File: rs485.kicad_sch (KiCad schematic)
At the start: 1 part

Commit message: add
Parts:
- added J1: Conn_01x04_Pin, symbol Connector:Conn_01x04_Pin
- added J2: Conn_01x04_Socket, symbol Connector:Conn_01x04_Socket
- added U2: SN74CB3Q3384APW, Package_SO:TSSOP-24_4.4x7.8mm_P0.65mm, symbol 74xx:SN74CB3Q3384APW
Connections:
- net at U1.1 (R): now also U1.4 (D), U2.3 (1A1)
- net at U1.2 (RE~): now also U1.3 (DE), U2.4 (1A2)
- net GND: now reaches U1.5 (GND)
- net GND: now also J1.4 (Pin_4), U2.12 (GND)
- net at U1.6 (B): now also J1.2 (Pin_2)
- net at U1.7 (A): now also J1.1 (Pin_1)
- net +5V: now reaches U1.8 (VCC)
- net +5V: now also J1.3 (Pin_3), U2.24 (VCC)
- new net: J2.3 (Pin_3), U2.1 (~{1OE})
- new net: J2.4 (Pin_4), U2.13 (~{2OE})
- new net: J2.1 (Pin_1), U2.2 (1B1)
- new net: J2.2 (Pin_2), U2.5 (1B2)

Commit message: sch of.
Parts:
- removed J2: Conn_01x04_Socket, symbol Connector:Conn_01x04_Socket
- added J2: Conn_01x04_Pin, symbol Connector:Conn_01x04_Pin
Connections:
- net GND: now also J2.1 (Pin_1); no longer J1.4 (Pin_4)
- net at U2.1 (~{1OE}): now also J1.3 (Pin_3)
- net at U2.13 (~{2OE}): now also J1.4 (Pin_4)
- net at U2.2 (1B1): now also J1.1 (Pin_1)
- net at U1.1 (R), U1.4 (D): now also U2.4 (1A2); no longer U2.3 (1A1)
- net at U1.2 (RE~), U1.3 (DE): now also U2.3 (1A1); no longer U2.4 (1A2)
- net at U2.5 (1B2): now also J1.2 (Pin_2)
- net at U1.6 (B): now also J2.3 (Pin_3); no longer J1.2 (Pin_2)
- net at U1.7 (A): now also J2.4 (Pin_4); no longer J1.1 (Pin_1)
- net +5V renamed VCC
- net VCC: now also J2.2 (Pin_2); no longer J1.3 (Pin_3)

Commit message: sch ok.
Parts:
- removed J1, J2: Conn_01x04_Pin, symbol Connector:Conn_01x04_Pin
- added J1, J3: Conn_01x12_Pin, symbol Connector:Conn_01x12_Pin
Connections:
- net GND: now also J1.9 (Pin_9)
- net VCC: now also J1.10 (Pin_10)
- net at U1.6 (B): now also J1.11 (Pin_11)
- net at U1.7 (A): now also J1.12 (Pin_12)
- net at U2.2 (1B1): now also J3.1 (Pin_1)
- net at U2.5 (1B2): now also J3.2 (Pin_2)
- net at U2.1 (~{1OE}): now also J3.11 (Pin_11)
- net at U2.13 (~{2OE}): now also J3.12 (Pin_12)
- net at U2.10 (1B5): now also J1.6 (Pin_6)
- net at U2.11 (1A5): now also J3.5 (Pin_5)
- net at U2.14 (2A1): now also J3.6 (Pin_6)
- net at U2.15 (2B1): now also J1.5 (Pin_5)
- net at U2.16 (2B2): now also J1.4 (Pin_4)
- net at U2.17 (2A2): now also J3.7 (Pin_7)
- net at U2.18 (2A3): now also J3.8 (Pin_8)
- net at U2.19 (2B3): now also J1.3 (Pin_3)
- net at U2.20 (2B4): now also J1.2 (Pin_2)
- net at U2.21 (2A4): now also J3.9 (Pin_9)
- net at U2.22 (2A5): now also J3.10 (Pin_10)
- net at U2.23 (2B5): now also J1.1 (Pin_1)
- net at U2.6 (1B3): now also J1.8 (Pin_8)
- net at U2.7 (1A3): now also J3.3 (Pin_3)
- net at U2.8 (1A4): now also J3.4 (Pin_4)
- net at U2.9 (1B4): now also J1.7 (Pin_7)

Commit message: up/.
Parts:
- U1: footprint (none) -> SOIC127P600X175-8N:SOIC127P600X175-8N
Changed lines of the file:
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@@
       (effects (font (size 1.27 1.27)))
     )
-    (property "Footprint" "" (at 114.3 54.61 0)
+    (property "Footprint" "SOIC127P600X175-8N:SOIC127P600X175-8N" (at 114.3 54.61 0)
       (effects (font (size 1.27 1.27)) hide)
     )

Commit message: add pcb file.
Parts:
- J1, J3: footprint (none) -> Connector_PinHeader_2.54mm:PinHeader_1x12_P2.54mm_Vertical
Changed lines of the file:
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@@
       (effects (font (size 1.27 1.27)))
     )
-    (property "Footprint" "" (at 41.91 96.52 0)
+    (property "Footprint" "Connector_PinHeader_2.54mm:PinHeader_1x12_P2.54mm_Vertical" (at 41.91 96.52 0)
       (effects (font (size 1.27 1.27)) hide)
     )
@@
       (effects (font (size 1.27 1.27)) (justify right))
     )
-    (property "Footprint" "" (at 204.47 74.93 0)
+    (property "Footprint" "Connector_PinHeader_2.54mm:PinHeader_1x12_P2.54mm_Vertical" (at 204.47 74.93 0)
       (effects (font (size 1.27 1.27)) hide)
     )

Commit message: pcb
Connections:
- net VCC: now also J1.12 (Pin_12); no longer J1.10 (Pin_10)
- net at U1.6 (B): now also J1.10 (Pin_10); no longer J1.11 (Pin_11)
- net at U1.7 (A): now also J1.11 (Pin_11); no longer J1.12 (Pin_12)
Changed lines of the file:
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@@
     (stroke (width 0) (type default))
   )
-  (wire (pts (xy 154.94 57.15) (xy 173.99 57.15))
+  (wire (pts (xy 154.94 57.15) (xy 179.07 57.15))
     (stroke (width 0) (type default))
   )
@@
     (stroke (width 0) (type default))
   )
+  (wire (pts (xy 175.26 59.69) (xy 175.26 62.23))
+    (stroke (width 0) (type default))
+  )
   (wire (pts (xy 128.27 102.87) (xy 176.53 102.87))
     (stroke (width 0) (type default))
@@
     (stroke (width 0) (type default))
   )
+  (wire (pts (xy 165.1 64.77) (xy 165.1 62.23))
+    (stroke (width 0) (type default))
+  )
   (wire (pts (xy 93.98 85.09) (xy 93.98 87.63))
     (stroke (width 0) (type default))
@@
     (stroke (width 0) (type default))
   )
+  (wire (pts (xy 123.19 59.69) (xy 175.26 59.69))
+    (stroke (width 0) (type default))
+  )
+  (wire (pts (xy 175.26 62.23) (xy 199.39 62.23))
+    (stroke (width 0) (type default))
+  )
   (wire (pts (xy 90.17 104.14) (xy 90.17 102.87))
     (stroke (width 0) (type default))
   )
-  (wire (pts (xy 123.19 62.23) (xy 199.39 62.23))
-    (stroke (width 0) (type default))
-  )
   (wire (pts (xy 46.99 109.22) (xy 88.9 109.22))
     (stroke (width 0) (type default))
@@
     (stroke (width 0) (type default))
   )
-  (wire (pts (xy 173.99 64.77) (xy 199.39 64.77))
-    (stroke (width 0) (type default))
-  )
   (wire (pts (xy 142.24 127) (xy 142.24 138.43))
     (stroke (width 0) (type default))
@@
     (stroke (width 0) (type default))
   )
+  (wire (pts (xy 179.07 59.69) (xy 179.07 57.15))
+    (stroke (width 0) (type default))
+  )
   (wire (pts (xy 180.34 105.41) (xy 180.34 87.63))
     (stroke (width 0) (type default))
@@
     (stroke (width 0) (type default))
   )
-  (wire (pts (xy 173.99 57.15) (xy 173.99 64.77))
-    (stroke (width 0) (type default))
-  )
   (wire (pts (xy 167.64 95.25) (xy 167.64 77.47))
     (stroke (width 0) (type default))
@@
     (stroke (width 0) (type default))
   )
+  (wire (pts (xy 199.39 64.77) (xy 165.1 64.77))
+    (stroke (width 0) (type default))
+  )
   (wire (pts (xy 105.41 59.69) (xy 100.33 59.69))
     (stroke (width 0) (type default))
@@
     (stroke (width 0) (type default))
   )
+  (wire (pts (xy 199.39 59.69) (xy 179.07 59.69))
+    (stroke (width 0) (type default))
+  )
   (wire (pts (xy 162.56 72.39) (xy 199.39 72.39))
     (stroke (width 0) (type default))
@@
     (stroke (width 0) (type default))
   )
-  (wire (pts (xy 123.19 59.69) (xy 199.39 59.69))
-    (stroke (width 0) (type default))
-  )
   (wire (pts (xy 80.01 90.17) (xy 80.01 93.98))
     (stroke (width 0) (type default))
@@
     (stroke (width 0) (type default))
   )
+  (wire (pts (xy 165.1 62.23) (xy 123.19 62.23))
+    (stroke (width 0) (type default))
+  )

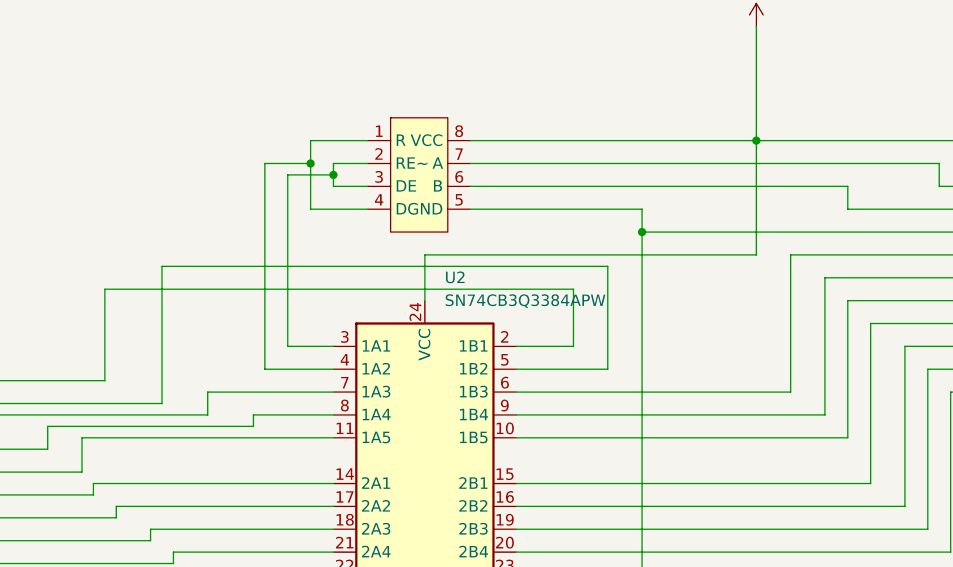
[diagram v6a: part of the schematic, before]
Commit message: 之前的没问题，现在重新设计，重新制作一个，加电源稳压的电容。
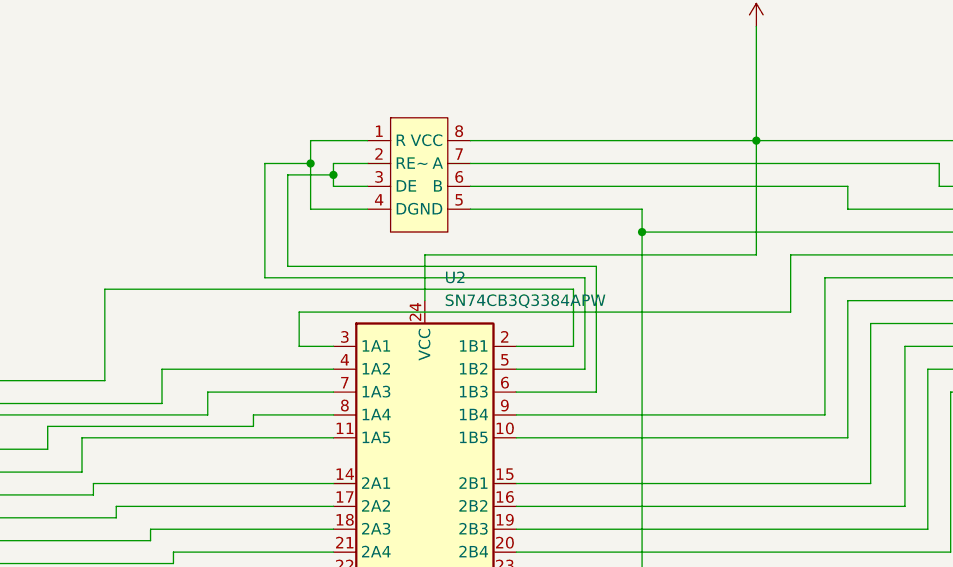
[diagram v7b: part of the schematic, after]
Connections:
- net at U1.1 (R), U1.4 (D): now also U2.5 (1B2); no longer U2.4 (1A2)
- net at U1.2 (RE~), U1.3 (DE): now also U2.6 (1B3); no longer U2.3 (1A1)
- net at J3.2 (Pin_2): now also U2.4 (1A2); no longer U2.5 (1B2)
- net at J1.8 (Pin_8): now also U2.3 (1A1); no longer U2.6 (1B3)
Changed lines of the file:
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@@
   (junction (at 107.95 60.96) (diameter 0) (color 0 0 0 0)
   )
+  (junction (at 142.24 127) (diameter 0) (color 0 0 0 0)
+  )
   (junction (at 105.41 59.69) (diameter 0) (color 0 0 0 0)
   )
-  (junction (at 142.24 127) (diameter 0) (color 0 0 0 0)
-  )
   (junction (at 142.24 67.31) (diameter 0) (color 0 0 0 0)
   )
-  (wire (pts (xy 138.43 71.12) (xy 88.9 71.12))
-    (stroke (width 0) (type default))
-  )
   (wire (pts (xy 69.85 88.9) (xy 46.99 88.9))
     (stroke (width 0) (type default))
@@
     (stroke (width 0) (type default))
   )
+  (wire (pts (xy 158.75 76.2) (xy 104.14 76.2))
+    (stroke (width 0) (type default))
+  )
   (wire (pts (xy 142.24 64.77) (xy 142.24 67.31))
     (stroke (width 0) (type default))
@@
     (stroke (width 0) (type default))
   )
-  (wire (pts (xy 107.95 80.01) (xy 102.87 80.01))
-    (stroke (width 0) (type default))
-  )
   (wire (pts (xy 107.95 95.25) (xy 81.28 95.25))
     (stroke (width 0) (type default))
@@
     (stroke (width 0) (type default))
   )
+  (wire (pts (xy 102.87 60.96) (xy 102.87 71.12))
+    (stroke (width 0) (type default))
+  )
   (wire (pts (xy 105.41 57.15) (xy 105.41 59.69))
     (stroke (width 0) (type default))
@@
     (stroke (width 0) (type default))
   )
-  (wire (pts (xy 88.9 71.12) (xy 88.9 86.36))
+  (wire (pts (xy 134.62 73.66) (xy 82.55 73.66))
+    (stroke (width 0) (type default))
+  )
+  (wire (pts (xy 107.95 97.79) (xy 83.82 97.79))
+    (stroke (width 0) (type default))
+  )
+  (wire (pts (xy 162.56 87.63) (xy 162.56 72.39))
+    (stroke (width 0) (type default))
+  )
+  (wire (pts (xy 105.41 64.77) (xy 111.76 64.77))
+    (stroke (width 0) (type default))
+  )
+  (wire (pts (xy 137.16 71.12) (xy 137.16 85.09))
+    (stroke (width 0) (type default))
+  )
+  (wire (pts (xy 173.99 100.33) (xy 173.99 82.55))
+    (stroke (width 0) (type default))
+  )
+  (wire (pts (xy 107.95 90.17) (xy 80.01 90.17))
     (stroke (width 0) (type default))
   )
@@
     (stroke (width 0) (type default))
   )
-  (wire (pts (xy 134.62 73.66) (xy 82.55 73.66))
-    (stroke (width 0) (type default))
-  )
-  (wire (pts (xy 107.95 97.79) (xy 83.82 97.79))
-    (stroke (width 0) (type default))
-  )
-  (wire (pts (xy 162.56 87.63) (xy 162.56 72.39))
-    (stroke (width 0) (type default))
-  )
-  (wire (pts (xy 105.41 64.77) (xy 111.76 64.77))
-    (stroke (width 0) (type default))
-  )
-  (wire (pts (xy 173.99 100.33) (xy 173.99 82.55))
-    (stroke (width 0) (type default))
-  )
-  (wire (pts (xy 107.95 90.17) (xy 80.01 90.17))
-    (stroke (width 0) (type default))
-  )
   (wire (pts (xy 134.62 80.01) (xy 134.62 73.66))
     (stroke (width 0) (type default))
@@
     (stroke (width 0) (type default))
   )
-  (wire (pts (xy 128.27 82.55) (xy 138.43 82.55))
-    (stroke (width 0) (type default))
-  )
   (wire (pts (xy 80.01 93.98) (xy 46.99 93.98))
     (stroke (width 0) (type default))
   )
+  (wire (pts (xy 102.87 71.12) (xy 137.16 71.12))
+    (stroke (width 0) (type default))
+  )
   (wire (pts (xy 107.95 110.49) (xy 88.9 110.49))
     (stroke (width 0) (type default))
   )
-  (wire (pts (xy 138.43 71.12) (xy 138.43 82.55))
-    (stroke (width 0) (type default))
-  )
   (wire (pts (xy 176.53 102.87) (xy 176.53 85.09))
     (stroke (width 0) (type default))
@@
     (stroke (width 0) (type default))
   )
-  (wire (pts (xy 158.75 85.09) (xy 158.75 69.85))
+  (wire (pts (xy 88.9 82.55) (xy 88.9 86.36))
     (stroke (width 0) (type default))
   )
@@
     (stroke (width 0) (type default))
   )
-  (wire (pts (xy 102.87 80.01) (xy 102.87 60.96))
+  (wire (pts (xy 100.33 59.69) (xy 105.41 59.69))
     (stroke (width 0) (type default))
   )
@@
     (stroke (width 0) (type default))
   )
+  (wire (pts (xy 100.33 72.39) (xy 100.33 59.69))
+    (stroke (width 0) (type default))
+  )
   (wire (pts (xy 165.1 90.17) (xy 165.1 74.93))
     (stroke (width 0) (type default))
@@
     (stroke (width 0) (type default))
   )
+  (wire (pts (xy 104.14 76.2) (xy 104.14 80.01))
+    (stroke (width 0) (type default))
+  )
+  (wire (pts (xy 128.27 82.55) (xy 135.89 82.55))
+    (stroke (width 0) (type default))
+  )
   (wire (pts (xy 128.27 80.01) (xy 134.62 80.01))
     (stroke (width 0) (type default))
@@
     (stroke (width 0) (type default))
   )
+  (wire (pts (xy 104.14 80.01) (xy 107.95 80.01))
+    (stroke (width 0) (type default))
+  )
   (wire (pts (xy 99.06 88.9) (xy 76.2 88.9))
     (stroke (width 0) (type default))
   )
+  (wire (pts (xy 137.16 85.09) (xy 128.27 85.09))
+    (stroke (width 0) (type default))
+  )
   (wire (pts (xy 93.98 87.63) (xy 69.85 87.63))
     (stroke (width 0) (type default))
@@
     (stroke (width 0) (type default))
   )
+  (wire (pts (xy 88.9 82.55) (xy 107.95 82.55))
+    (stroke (width 0) (type default))
+  )
   (wire (pts (xy 154.94 57.15) (xy 123.19 57.15))
     (stroke (width 0) (type default))
   )
-  (wire (pts (xy 100.33 82.55) (xy 107.95 82.55))
-    (stroke (width 0) (type default))
-  )
   (wire (pts (xy 88.9 109.22) (xy 88.9 110.49))
     (stroke (width 0) (type default))
   )
+  (wire (pts (xy 158.75 69.85) (xy 158.75 76.2))
+    (stroke (width 0) (type default))
+  )
   (wire (pts (xy 167.64 95.25) (xy 167.64 77.47))
     (stroke (width 0) (type default))
   )
-  (wire (pts (xy 100.33 59.69) (xy 100.33 82.55))
-    (stroke (width 0) (type default))
-  )
-  (wire (pts (xy 128.27 85.09) (xy 158.75 85.09))
+  (wire (pts (xy 135.89 72.39) (xy 100.33 72.39))
     (stroke (width 0) (type default))
   )
@@
     (stroke (width 0) (type default))
   )
-  (wire (pts (xy 105.41 59.69) (xy 100.33 59.69))
-    (stroke (width 0) (type default))
-  )
   (wire (pts (xy 92.71 105.41) (xy 92.71 106.68))
     (stroke (width 0) (type default))
@@
     (stroke (width 0) (type default))
   )
+  (wire (pts (xy 135.89 82.55) (xy 135.89 72.39))
+    (stroke (width 0) (type default))
+  )

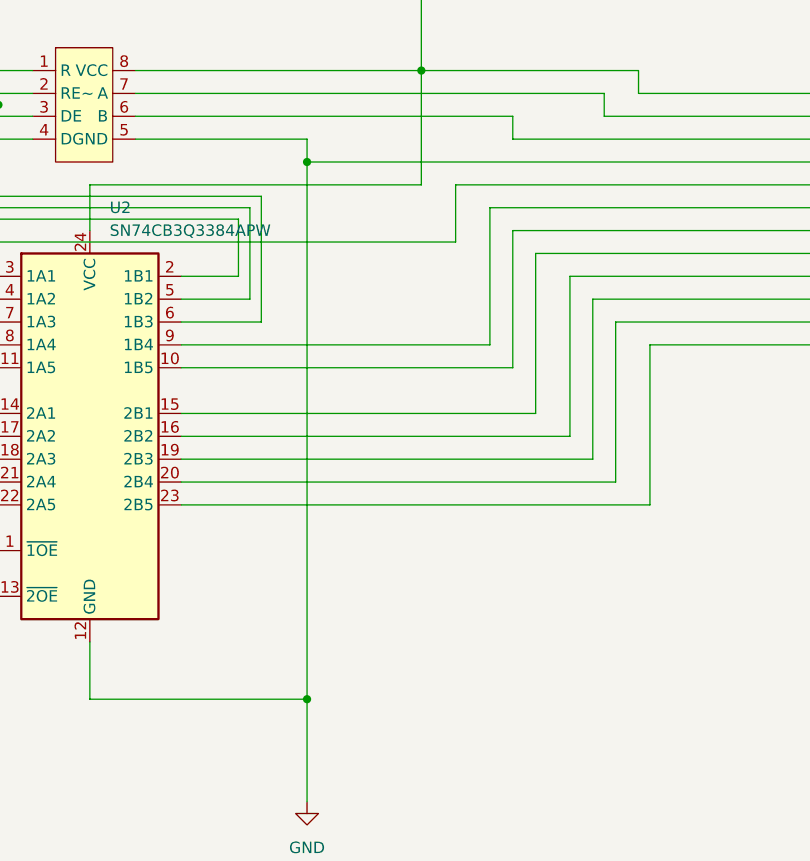
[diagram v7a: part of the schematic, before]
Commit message: update 原理图，增加滤波。电容。暂时先不进行。
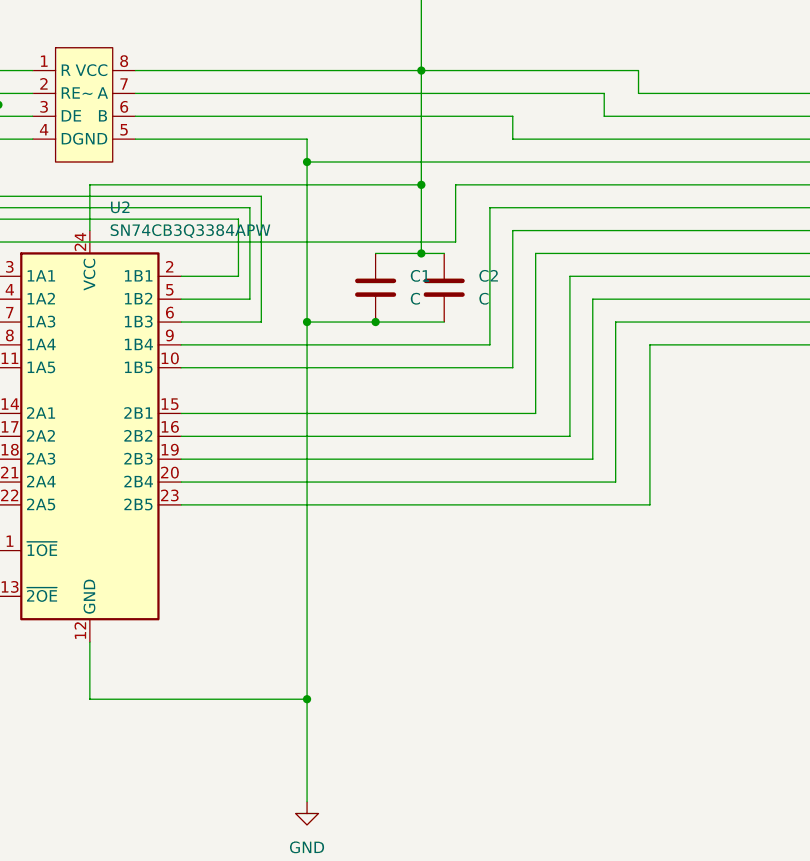
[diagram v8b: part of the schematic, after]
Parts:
- added C1, C2: C, symbol Device:C
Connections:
- net GND: now also C1.2, C2.2
- net VCC: now also C1.1, C2.1
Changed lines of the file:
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@@
   (junction (at 154.94 57.15) (diameter 0) (color 0 0 0 0)
   )
+  (junction (at 142.24 85.09) (diameter 0) (color 0 0 0 0)
+  )
   (junction (at 107.95 60.96) (diameter 0) (color 0 0 0 0)
   )
+  (junction (at 154.94 77.47) (diameter 0) (color 0 0 0 0)
+  )
   (junction (at 142.24 127) (diameter 0) (color 0 0 0 0)
   )
   (junction (at 105.41 59.69) (diameter 0) (color 0 0 0 0)
   )
+  (junction (at 154.94 69.85) (diameter 0) (color 0 0 0 0)
+  )
   (junction (at 142.24 67.31) (diameter 0) (color 0 0 0 0)
   )
+  (junction (at 149.86 85.09) (diameter 0) (color 0 0 0 0)
+  )
   (wire (pts (xy 69.85 88.9) (xy 46.99 88.9))
     (stroke (width 0) (type default))
@@
     (stroke (width 0) (type default))
   )
+  (wire (pts (xy 154.94 77.47) (xy 149.86 77.47))
+    (stroke (width 0) (type default))
+  )
   (wire (pts (xy 102.87 60.96) (xy 102.87 71.12))
     (stroke (width 0) (type default))
   )
+  (wire (pts (xy 154.94 77.47) (xy 157.48 77.47))
+    (stroke (width 0) (type default))
+  )
   (wire (pts (xy 105.41 57.15) (xy 105.41 59.69))
     (stroke (width 0) (type default))
@@
     (stroke (width 0) (type default))
   )
+  (wire (pts (xy 142.24 85.09) (xy 142.24 127))
+    (stroke (width 0) (type default))
+  )
   (wire (pts (xy 180.34 87.63) (xy 199.39 87.63))
     (stroke (width 0) (type default))
@@
     (stroke (width 0) (type default))
   )
+  (wire (pts (xy 149.86 85.09) (xy 157.48 85.09))
+    (stroke (width 0) (type default))
+  )
   (wire (pts (xy 102.87 71.12) (xy 137.16 71.12))
     (stroke (width 0) (type default))
@@
     (stroke (width 0) (type default))
   )
-  (wire (pts (xy 142.24 67.31) (xy 142.24 127))
+  (wire (pts (xy 142.24 67.31) (xy 142.24 85.09))
     (stroke (width 0) (type default))
   )
@@
     (stroke (width 0) (type default))
   )
+  (wire (pts (xy 154.94 69.85) (xy 154.94 77.47))
+    (stroke (width 0) (type default))
+  )
   (wire (pts (xy 92.71 106.68) (xy 46.99 106.68))
     (stroke (width 0) (type default))
@@
   )
   (wire (pts (xy 68.58 115.57) (xy 107.95 115.57))
+    (stroke (width 0) (type default))
+  )
+  (wire (pts (xy 142.24 85.09) (xy 149.86 85.09))
     (stroke (width 0) (type default))
   )
@@
         (path "/cdd6915d-d11c-4d9a-9788-927b18e5b701"
           (reference "#PWR02") (unit 1)
+        )
+      )
+    )
+  )
+  (symbol (lib_id "Device:C") (at 149.86 81.28 0) (unit 1)
+    (in_bom yes) (on_board yes) (dnp no) (fields_autoplaced)
+    (property "Reference" "C1" (at 153.67 80.01 0)
+      (effects (font (size 1.27 1.27)) (justify left))
+    )
+    (property "Value" "C" (at 153.67 82.55 0)
+      (effects (font (size 1.27 1.27)) (justify left))
+    )
+    (property "Footprint" "" (at 150.8252 85.09 0)
+      (effects (font (size 1.27 1.27)) hide)
+    )
+    (property "Datasheet" "~" (at 149.86 81.28 0)
+      (effects (font (size 1.27 1.27)) hide)
+    )
+    (pin "1")
+    (pin "2")
+    (instances
+      (project "rs485"
+        (path "/cdd6915d-d11c-4d9a-9788-927b18e5b701"
+          (reference "C1") (unit 1)
         )
       )
@@
         )
       )
+    )
+  )
+  (symbol (lib_id "Device:C") (at 157.48 81.28 0) (unit 1)
+    (in_bom yes) (on_board yes) (dnp no) (fields_autoplaced)
+    (property "Reference" "C2" (at 161.29 80.01 0)
+      (effects (font (size 1.27 1.27)) (justify left))
+    )
+    (property "Value" "C" (at 161.29 82.55 0)
+      (effects (font (size 1.27 1.27)) (justify left))
+    )
+    (property "Footprint" "" (at 158.4452 85.09 0)
+      (effects (font (size 1.27 1.27)) hide)
+    )
+    (property "Datasheet" "~" (at 157.48 81.28 0)
+      (effects (font (size 1.27 1.27)) hide)
+    )
+    (pin "1")
+    (pin "2")
+    (instances
+      (project "rs485"
+        (path "/cdd6915d-d11c-4d9a-9788-927b18e5b701"
+          (reference "C2") (unit 1)
+        )
+      )
